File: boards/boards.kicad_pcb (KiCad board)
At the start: 2 copper layers, 34 parts, among them J1 MicroSD, P1 CONN_01X04, P10 , P11 , P12 , P13 CONN_01X02, P2 , P3 , P4 , P5 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

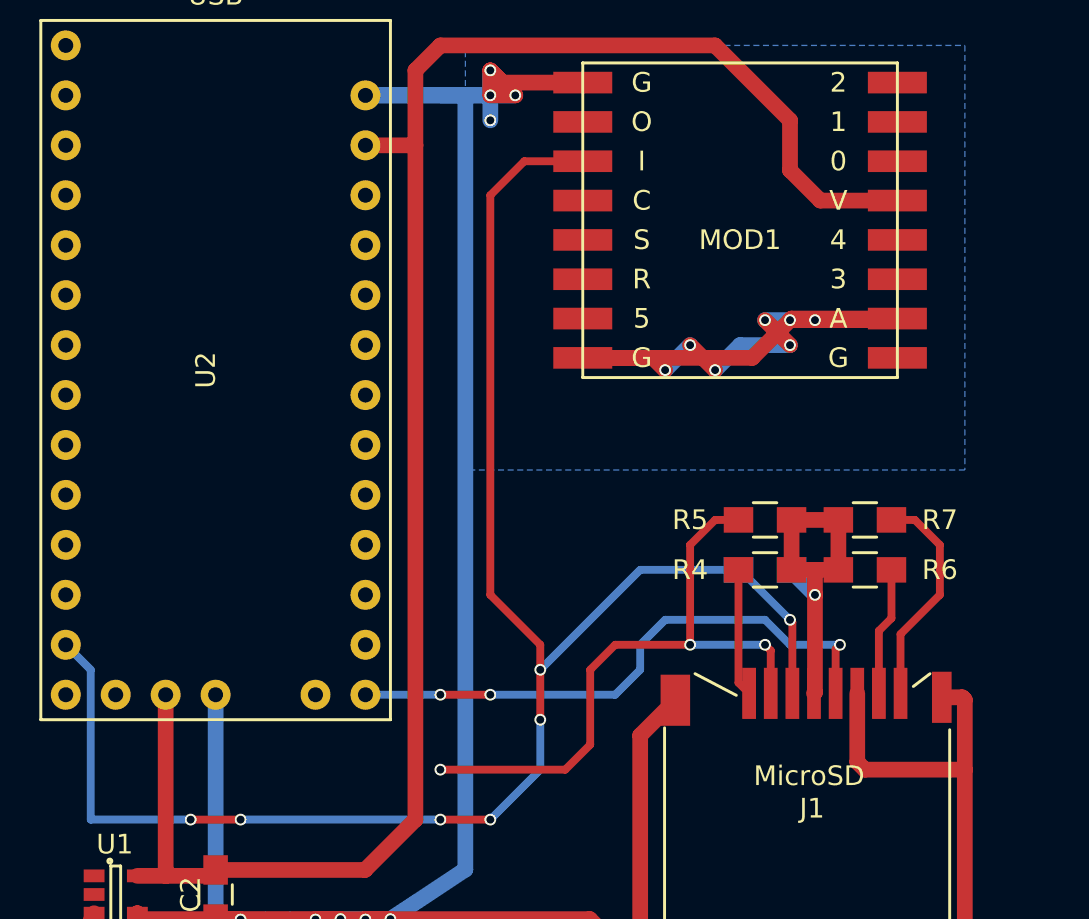
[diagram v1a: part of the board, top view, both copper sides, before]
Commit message: Completed SPI connections
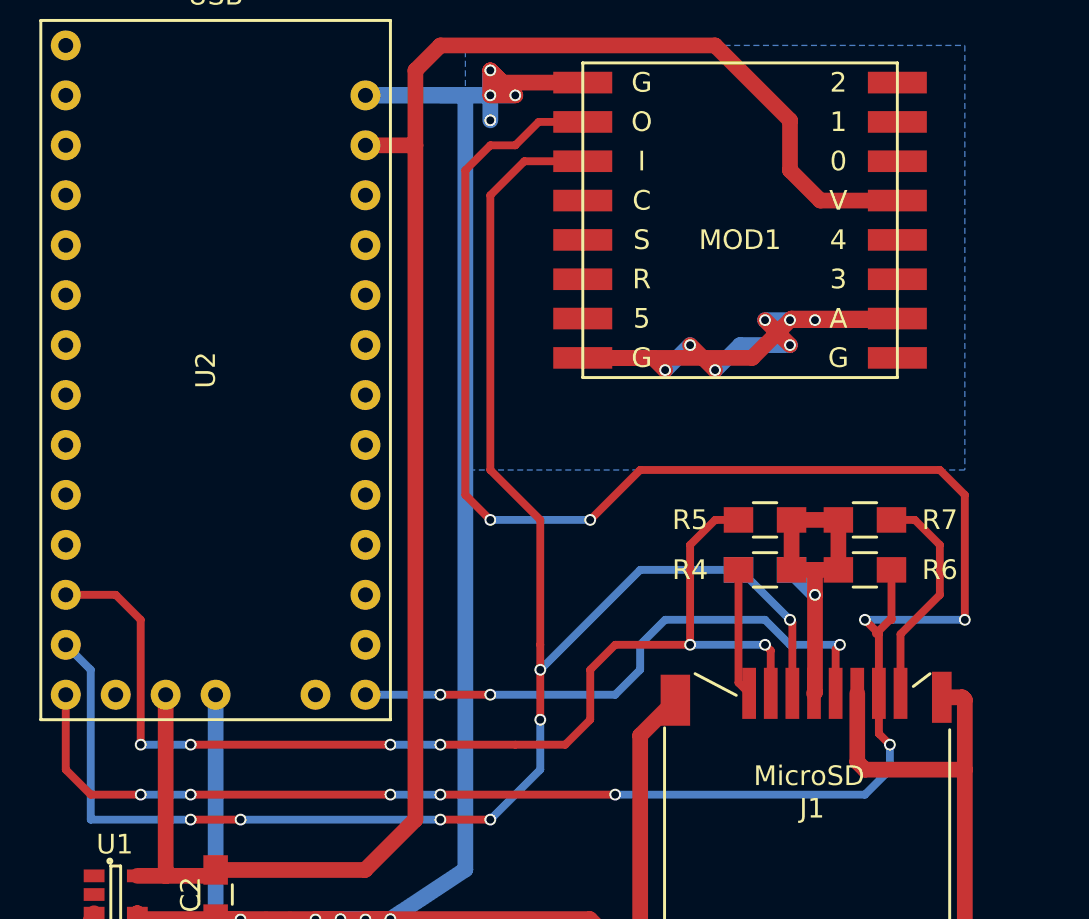
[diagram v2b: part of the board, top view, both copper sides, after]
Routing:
- net Net-(J1-Pad7): track 6.55 -> 121.2 mm, vias 0 -> 10
- net Net-(J1-Pad2): track 32.0 -> 56.7 mm, vias 3 -> 6
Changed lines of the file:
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@@
   (general
     (links 77)
-    (no_connects 45)
-    (area 0 0 0 0)
+    (no_connects 42)
+    (area 46.889999 22.584999 157.728481 112.928601)
     (thickness 1.6)
     (drawings 4)
-    (tracks 186)
+    (tracks 234)
     (zones 0)
     (modules 34)
@@
   (segment (start 50.65 68.58) (end 50.97 68.26) (width 0.5) (layer F.Cu) (net 2))
   (segment (start 50.97 70.97) (end 50.82 71.12) (width 0.5) (layer F.Cu) (net 2))
-  (segment (start 86.44 50.8) (end 86.44 50.88) (width 0.8) (layer B.Cu) (net 3) (status C00000))
-  (segment (start 86.44 50.88) (end 87.63 52.07) (width 0.8) (layer B.Cu) (net 3) (status 400000))
+  (segment (start 86.44 50.8) (end 86.44 50.88) (width 0.8) (layer B.Cu) (net 3))
+  (segment (start 86.44 50.88) (end 87.63 52.07) (width 0.8) (layer B.Cu) (net 3))
   (via (at 87.63 52.07) (size 0.6) (drill 0.4) (layers F.Cu B.Cu) (net 3))
   (segment (start 87.63 50.8) (end 87.63 52.07) (width 0.8) (layer F.Cu) (net 3))
@@
   (segment (start 83.74 50.8) (end 83.74 56.54) (width 0.4) (layer F.Cu) (net 9))
   (segment (start 83.74 56.54) (end 84.28 57.08) (width 0.4) (layer F.Cu) (net 9))
-  (via (at 68.58 60.96) (size 0.6) (drill 0.4) (layers F.Cu B.Cu) (net 10))
-  (segment (start 68.58 60.96) (end 74.93 60.96) (width 0.4) (layer F.Cu) (net 10))
-  (segment (start 74.93 60.96) (end 76.2 59.69) (width 0.4) (layer F.Cu) (net 10))
-  (segment (start 76.2 59.69) (end 76.2 55.88) (width 0.4) (layer F.Cu) (net 10))
+  (segment (start 72.39 59.69) (end 74.93 59.69) (width 0.4) (layer F.Cu) (net 10))
+  (segment (start 52.07 52.07) (end 53.34 53.34) (width 0.4) (layer F.Cu) (net 10))
+  (segment (start 53.34 53.34) (end 53.34 59.69) (width 0.4) (layer F.Cu) (net 10))
+  (via (at 53.34 59.69) (size 0.6) (drill 0.4) (layers F.Cu B.Cu) (net 10))
+  (segment (start 53.34 59.69) (end 55.88 59.69) (width 0.4) (layer B.Cu) (net 10))
+  (via (at 55.88 59.69) (size 0.6) (drill 0.4) (layers F.Cu B.Cu) (net 10))
+  (segment (start 55.88 59.69) (end 66.04 59.69) (width 0.4) (layer F.Cu) (net 10))
+  (via (at 66.04 59.69) (size 0.6) (drill 0.4) (layers F.Cu B.Cu) (net 10))
+  (segment (start 66.04 59.69) (end 68.58 59.69) (width 0.4) (layer B.Cu) (net 10))
+  (via (at 68.58 59.69) (size 0.6) (drill 0.4) (layers F.Cu B.Cu) (net 10))
+  (segment (start 68.58 59.69) (end 72.39 59.69) (width 0.4) (layer F.Cu) (net 10))
   (segment (start 76.2 55.88) (end 77.47 54.61) (width 0.4) (layer F.Cu) (net 10))
   (segment (start 81.28 54.61) (end 77.47 54.61) (width 0.4) (layer F.Cu) (net 10))
+  (segment (start 52.07 52.07) (end 49.53 52.07) (width 0.4) (layer F.Cu) (net 10))
+  (segment (start 76.2 58.42) (end 76.2 55.88) (width 0.4) (layer F.Cu) (net 10))
+  (segment (start 74.93 59.69) (end 76.2 58.42) (width 0.4) (layer F.Cu) (net 10))
   (segment (start 83.74 48.26) (end 82.55 48.26) (width 0.4) (layer F.Cu) (net 10))
   (segment (start 82.55 48.26) (end 81.28 49.53) (width 0.4) (layer F.Cu) (net 10))
@@
   (segment (start 85.09 54.61) (end 85.38 54.9) (width 0.4) (layer F.Cu) (net 10))
   (segment (start 85.38 54.9) (end 85.38 57.08) (width 0.4) (layer F.Cu) (net 10))
+  (segment (start 73.66 48.26) (end 71.12 45.72) (width 0.4) (layer F.Cu) (net 11))
+  (segment (start 73.66 54.61) (end 73.66 48.26) (width 0.4) (layer F.Cu) (net 11))
+  (segment (start 71.12 45.72) (end 71.12 31.75) (width 0.4) (layer F.Cu) (net 11))
   (segment (start 73.66 55.88) (end 73.66 54.61) (width 0.4) (layer F.Cu) (net 11))
-  (segment (start 72.85 30.02) (end 75.82 30.02) (width 0.4) (layer F.Cu) (net 11) (status 800000))
+  (segment (start 72.85 30.02) (end 75.82 30.02) (width 0.4) (layer F.Cu) (net 11))
   (segment (start 71.12 31.75) (end 72.85 30.02) (width 0.4) (layer F.Cu) (net 11))
-  (segment (start 71.12 52.07) (end 71.12 31.75) (width 0.4) (layer F.Cu) (net 11))
-  (segment (start 73.66 54.61) (end 71.12 52.07) (width 0.4) (layer F.Cu) (net 11))
-  (segment (start 49.53 54.61) (end 50.8 55.88) (width 0.4) (layer B.Cu) (net 11) (status 400000))
-  (segment (start 78.74 50.8) (end 83.74 50.8) (width 0.4) (layer B.Cu) (net 11) (status 800000))
+  (segment (start 49.53 54.61) (end 50.8 55.88) (width 0.4) (layer B.Cu) (net 11))
+  (segment (start 78.74 50.8) (end 83.74 50.8) (width 0.4) (layer B.Cu) (net 11))
   (segment (start 73.66 55.88) (end 78.74 50.8) (width 0.4) (layer B.Cu) (net 11))
   (via (at 73.66 55.88) (size 0.6) (drill 0.4) (layers F.Cu B.Cu) (net 11))
@@
   (segment (start 78.74 55.88) (end 78.74 54.61) (width 0.4) (layer B.Cu) (net 12))
   (segment (start 77.47 57.15) (end 78.74 55.88) (width 0.4) (layer B.Cu) (net 12))
-  (segment (start 91.52 50.8) (end 91.52 53.26) (width 0.4) (layer F.Cu) (net 13))
+  (segment (start 49.53 57.15) (end 49.53 60.96) (width 0.4) (layer F.Cu) (net 13) (status 400000))
+  (segment (start 90.88 59.13) (end 90.88 57.08) (width 0.4) (layer F.Cu) (net 13) (status 800000))
+  (segment (start 91.44 59.69) (end 90.88 59.13) (width 0.4) (layer F.Cu) (net 13))
+  (via (at 91.44 59.69) (size 0.6) (drill 0.4) (layers F.Cu B.Cu) (net 13))
+  (segment (start 91.44 60.96) (end 91.44 59.69) (width 0.4) (layer B.Cu) (net 13))
+  (segment (start 90.17 62.23) (end 91.44 60.96) (width 0.4) (layer B.Cu) (net 13))
+  (segment (start 77.47 62.23) (end 90.17 62.23) (width 0.4) (layer B.Cu) (net 13))
+  (via (at 77.47 62.23) (size 0.6) (drill 0.4) (layers F.Cu B.Cu) (net 13))
+  (segment (start 68.58 62.23) (end 77.47 62.23) (width 0.4) (layer F.Cu) (net 13))
+  (via (at 68.58 62.23) (size 0.6) (drill 0.4) (layers F.Cu B.Cu) (net 13))
+  (segment (start 66.04 62.23) (end 68.58 62.23) (width 0.4) (layer B.Cu) (net 13))
+  (via (at 66.04 62.23) (size 0.6) (drill 0.4) (layers F.Cu B.Cu) (net 13))
+  (segment (start 55.88 62.23) (end 66.04 62.23) (width 0.4) (layer F.Cu) (net 13))
+  (via (at 55.88 62.23) (size 0.6) (drill 0.4) (layers F.Cu B.Cu) (net 13))
+  (segment (start 53.34 62.23) (end 55.88 62.23) (width 0.4) (layer B.Cu) (net 13))
+  (via (at 53.34 62.23) (size 0.6) (drill 0.4) (layers F.Cu B.Cu) (net 13))
+  (segment (start 50.8 62.23) (end 53.34 62.23) (width 0.4) (layer F.Cu) (net 13))
+  (segment (start 49.53 60.96) (end 50.8 62.23) (width 0.4) (layer F.Cu) (net 13))
+  (via (at 76.2 48.26) (size 0.6) (drill 0.4) (layers F.Cu B.Cu) (net 13))
+  (segment (start 75.82 28.02) (end 73.58 28.02) (width 0.4) (layer F.Cu) (net 13))
+  (segment (start 73.58 28.02) (end 72.39 29.21) (width 0.4) (layer F.Cu) (net 13))
+  (segment (start 72.39 29.21) (end 71.12 29.21) (width 0.4) (layer F.Cu) (net 13))
+  (segment (start 71.12 29.21) (end 69.85 30.48) (width 0.4) (layer F.Cu) (net 13))
+  (segment (start 69.85 30.48) (end 69.85 46.99) (width 0.4) (layer F.Cu) (net 13))
+  (segment (start 69.85 46.99) (end 71.12 48.26) (width 0.4) (layer F.Cu) (net 13))
+  (via (at 71.12 48.26) (size 0.6) (drill 0.4) (layers F.Cu B.Cu) (net 13))
+  (segment (start 71.12 48.26) (end 76.2 48.26) (width 0.4) (layer B.Cu) (net 13))
+  (segment (start 90.88 54.05) (end 90.73 54.05) (width 0.4) (layer F.Cu) (net 13))
+  (segment (start 90.17 53.34) (end 90.88 54.05) (width 0.4) (layer F.Cu) (net 13))
+  (via (at 90.17 53.34) (size 0.6) (drill 0.4) (layers F.Cu B.Cu) (net 13))
+  (segment (start 95.25 53.34) (end 90.17 53.34) (width 0.4) (layer B.Cu) (net 13))
+  (via (at 95.25 53.34) (size 0.6) (drill 0.4) (layers F.Cu B.Cu) (net 13))
+  (segment (start 95.25 46.99) (end 95.25 53.34) (width 0.4) (layer F.Cu) (net 13))
+  (segment (start 93.98 45.72) (end 95.25 46.99) (width 0.4) (layer F.Cu) (net 13))
+  (segment (start 78.74 45.72) (end 93.98 45.72) (width 0.4) (layer F.Cu) (net 13))
+  (segment (start 76.2 48.26) (end 78.74 45.72) (width 0.4) (layer F.Cu) (net 13))
+  (segment (start 91.52 50.8) (end 91.52 53.34) (width 0.4) (layer F.Cu) (net 13))
+  (segment (start 91.52 53.34) (end 91.52 53.26) (width 0.4) (layer F.Cu) (net 13))
   (segment (start 91.52 53.26) (end 90.88 53.9) (width 0.4) (layer F.Cu) (net 13))
   (segment (start 90.88 53.9) (end 90.88 57.08) (width 0.4) (layer F.Cu) (net 13))

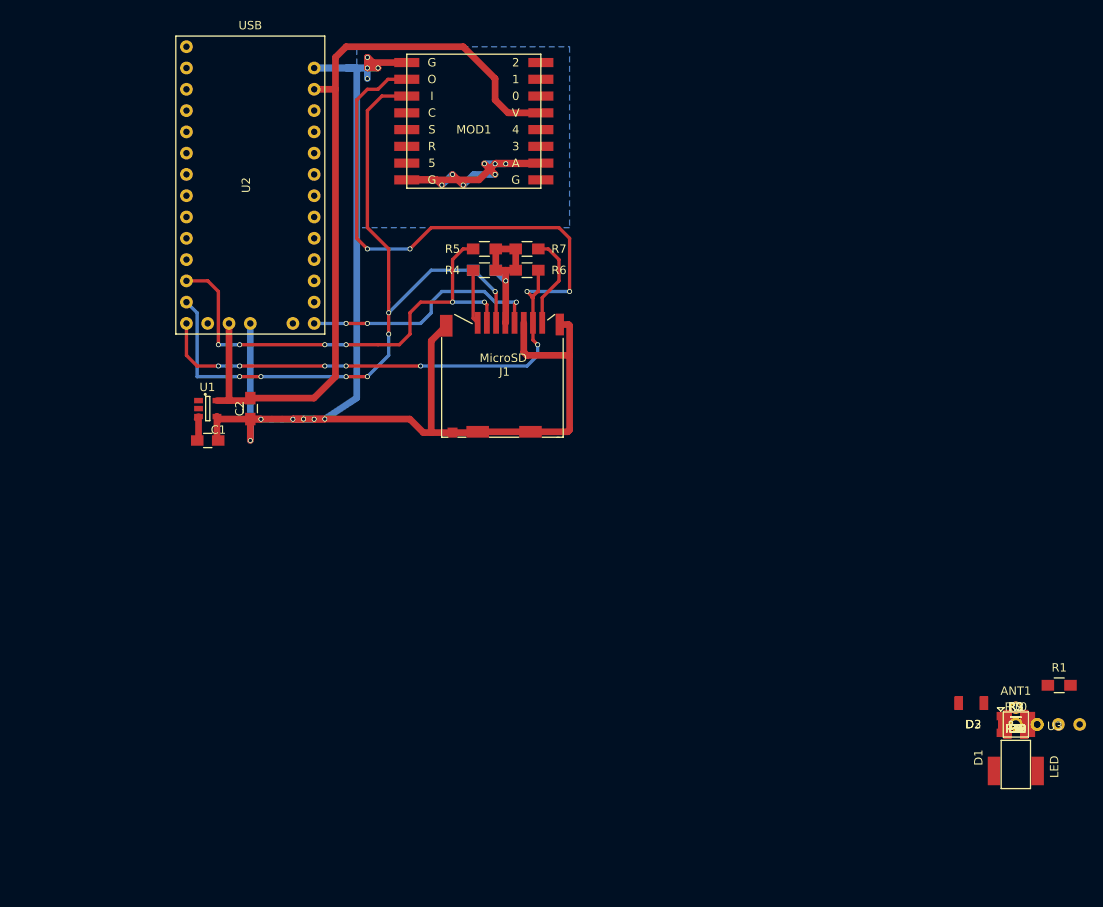
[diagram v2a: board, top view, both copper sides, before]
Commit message: Changed to TO252 power reg. Continued trace connection.
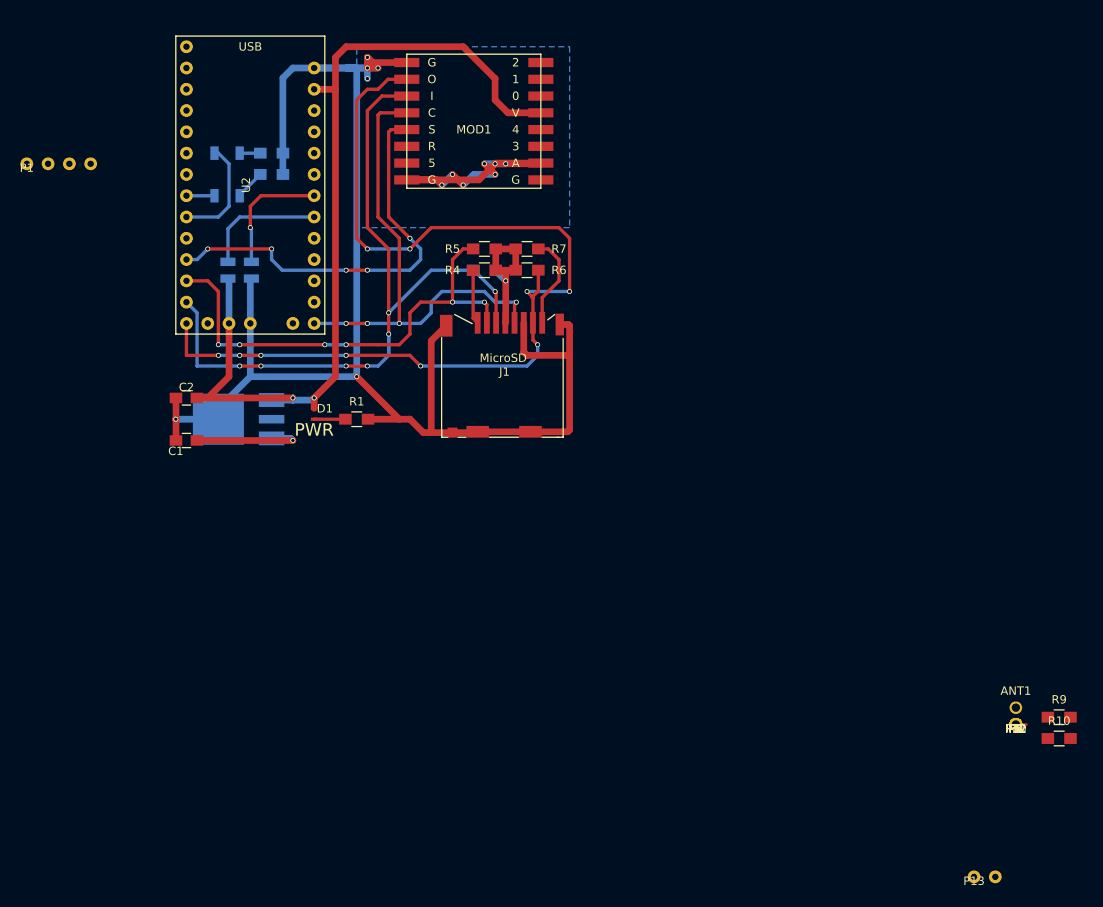
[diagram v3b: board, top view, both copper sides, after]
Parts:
- C1, C2: value (none) -> 4.7uF
- D1: footprint Parts:CONN_JST -> william-parts:KPH-1608SGC
- D2, D3, R2, R3, U3: moved to B.Cu
- R4, R5, R6, R7, R8: value (none) -> 47k
- U1: value (none) -> LP38690; footprint TO_SOT_Packages_SMD.pretty:SOT-23-5 -> TO_SOT_Packages_SMD.pretty:TO-252-3Lead; moved to B.Cu
- moved P1 135.7 mm to (30.5, 38.1)
- moved D3 113.5 mm to (59.7, 34.3)
- moved R3 112.0 mm to (59.7, 36.8)
- moved D2 110.4 mm to (59.7, 39.4)
- moved R2 110.4 mm to (59.7, 39.4)
- moved U3 107.3 mm to (55.9, 50.8)
- moved D1 90.1 mm to (68.6, 63.5), turned to 90 degrees
- moved R1 89.6 mm to (69.8, 68.6)
- moved P13 18.9 mm to (143.5, 123.2)
- moved C2 7.73 mm to (49.5, 66.0), turned to 180 degrees
- moved U1 7.73 mm to (59.7, 68.6), turned to 270 degrees
- moved R10 5.43 mm to (153.7, 106.7)
- moved R9 5.24 mm to (153.7, 104.1)
- moved C1 2.54 mm to (49.5, 71.1), turned to 180 degrees
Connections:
- U1 pad 1: VCC -> +3V3
- U1 pad 2: (no net) -> GND
- U1 pad 4: GND -> (no net)
- U2 pad 23: Net-(P12-Pad1) -> Net-(MOD1-Pad14)
- U2 pad 8: Net-(MOD1-Pad14) -> Net-(P12-Pad1)
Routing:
- net Net-(MOD1-Pad5): track 0.00 -> 49.9 mm, vias 0 -> 5
- net Net-(J1-Pad5): track 29.5 -> 59.0 mm, vias 3 -> 4
- net SCL: track 0.00 -> 14.8 mm, vias 0 -> 1
- net SDA: track 0.00 -> 14.8 mm
- net +3V3: track 113.9 -> 127.2 mm, vias 1 -> 3
- net Net-(D3-Pad2): track 0.00 -> 12.9 mm
- net VCC: track 3.80 -> 14.1 mm, vias 0 -> 1
- net GND: track 223.7 -> 228.3 mm, vias 17 -> 13
- net Net-(D1-Pad1): track 0.00 -> 3.73 mm
- net Net-(D2-Pad1): track 0.00 -> 3.56 mm
- net Net-(D2-Pad2): track 0.00 -> 3.35 mm
- net Net-(D3-Pad1): track 0.00 -> 2.46 mm
- net Net-(J1-Pad3): track 88.7 -> 89.4 mm
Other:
- board text added: "PWR"
- board text added: "RX/TX"
- board text added: "SD/GPS OK"

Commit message: Continued PCB layout.
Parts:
- R10, R9: moved to B.Cu
- moved R10 112.7 mm to (59.7, 44.5), turned to 90 degrees
- moved R9 109.2 mm to (62.2, 44.5), turned to 90 degrees
- moved ANT1 85.5 mm to (95.2, 38.1), turned to 180 degrees
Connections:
- ANT1 pad 3: (no net) -> Net-(ANT1-Pad1)
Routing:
- net Net-(MOD1-Pad14): track 0.00 -> 47.6 mm
- net Net-(MOD1-Pad6): track 0.00 -> 38.1 mm, vias 0 -> 3
- net GND: track 228.3 -> 192.1 mm, vias 13 -> 6
- net Net-(ANT1-Pad1): track 0.00 -> 3.46 mm
- net SCL: track 14.8 -> 17.4 mm, vias 1 -> 2
- net +3V3: track 127.2 -> 129.8 mm
- net SDA: track 14.8 -> 16.2 mm
- net Net-(J1-Pad7): track 121.2 -> 120.1 mm
- net (no net): vias 0 -> 1
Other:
- net class miniPWR added: clearance 0.2, trace_width 0.4, via_dia 0.6, via_drill 0.4
